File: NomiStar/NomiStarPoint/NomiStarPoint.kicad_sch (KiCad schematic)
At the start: 10 parts, among them J1 Conn_01x04

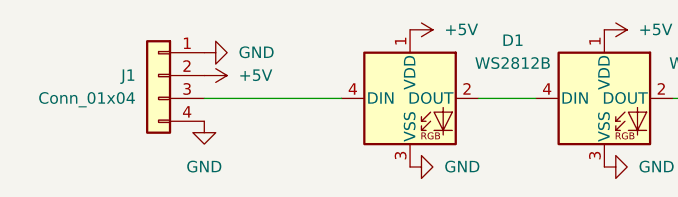
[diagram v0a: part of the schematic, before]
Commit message: Fixed swapped data in and +5v
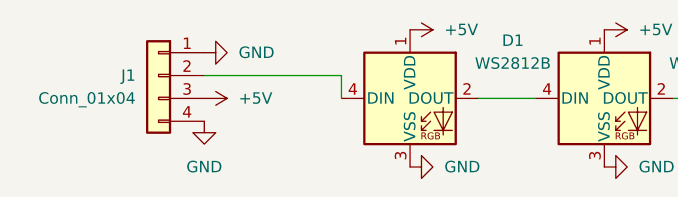
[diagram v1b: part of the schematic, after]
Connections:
- net +5V: now also J1.3 (Pin_3); no longer J1.2 (Pin_2)
- net at D1.4 (DIN): now also J1.2 (Pin_2); no longer J1.3 (Pin_3)
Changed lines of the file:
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@@
+	(wire
+		(pts
+			(xy 43.18 54.61) (xy 58.42 54.61)
+		)
+		(stroke
+			(width 0)
+			(type default)
+		)
+	)
 	(wire
 		(pts
@@
 	(wire
 		(pts
-			(xy 43.18 57.15) (xy 58.42 57.15)
+			(xy 58.42 54.61) (xy 58.42 57.15)
 		)
 		(stroke
@@
 	(symbol
 		(lib_id "power:+5V")
-		(at 43.18 54.61 270)
+		(at 43.18 57.15 270)
 		(unit 1)
 		(body_style 1)
@@
 		(fields_autoplaced yes)
 		(property "Reference" "#PWR03"
-			(at 39.37 54.61 0)
+			(at 39.37 57.15 0)
 			(hide yes)
 			(show_name no)
@@
 		)
 		(property "Value" "+5V"
-			(at 46.99 54.6099 90)
+			(at 46.99 57.1499 90)
 			(show_name no)
 			(do_not_autoplace no)
@@
 		)
 		(property "Footprint" ""
-			(at 43.18 54.61 0)
+			(at 43.18 57.15 0)
 			(hide yes)
 			(show_name no)
@@
 		)
 		(property "Datasheet" ""
-			(at 43.18 54.61 0)
+			(at 43.18 57.15 0)
 			(hide yes)
 			(show_name no)
@@
 		)
 		(property "Description" "Power symbol creates a global label with name \"+5V\""
-			(at 43.18 54.61 0)
-			(hide yes)
-			(show_name no)
+			(at 43.18 57.15 0)
+			(hide yes)
+			(show_name no)
